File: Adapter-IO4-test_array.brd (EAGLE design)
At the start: 107.6 x 107.6 mm, 72 parts, among them CON1X11 RJ12/6, CON1X12 RJ12/6, CON1X21 RJ12/6, CON1X22 RJ12/6, CON2X11 0.100, CON2X12 0.100, CON2X21 0.100, CON2X22 0.100, Q1X11 p-fet, Q1X12 p-fet, Q1X21 p-fet, Q1X22 p-fet, Q2X11 p-fet, Q2X12 p-fet, Q2X21 p-fet, Q2X22 p-fet, Q3X11 p-fet, Q3X12 p-fet, Q3X21 p-fet, Q3X22 p-fet, Q4X11 p-fet, Q4X12 p-fet, Q4X21 p-fet, Q4X22 p-fet, SW1X11 SPST-MOM, SW1X12 SPST-MOM, SW1X21 SPST-MOM, SW1X22 SPST-MOM, SW2X11 SPST-MOM, SW2X12 SPST-MOM, SW2X21 SPST-MOM, SW2X22 SPST-MOM, SW3X11 SPST-MOM, SW3X12 SPST-MOM, SW3X21 SPST-MOM, SW3X22 SPST-MOM, SW4X11 SPST-MOM, SW4X12 SPST-MOM, SW4X21 SPST-MOM, SW4X22 SPST-MOM

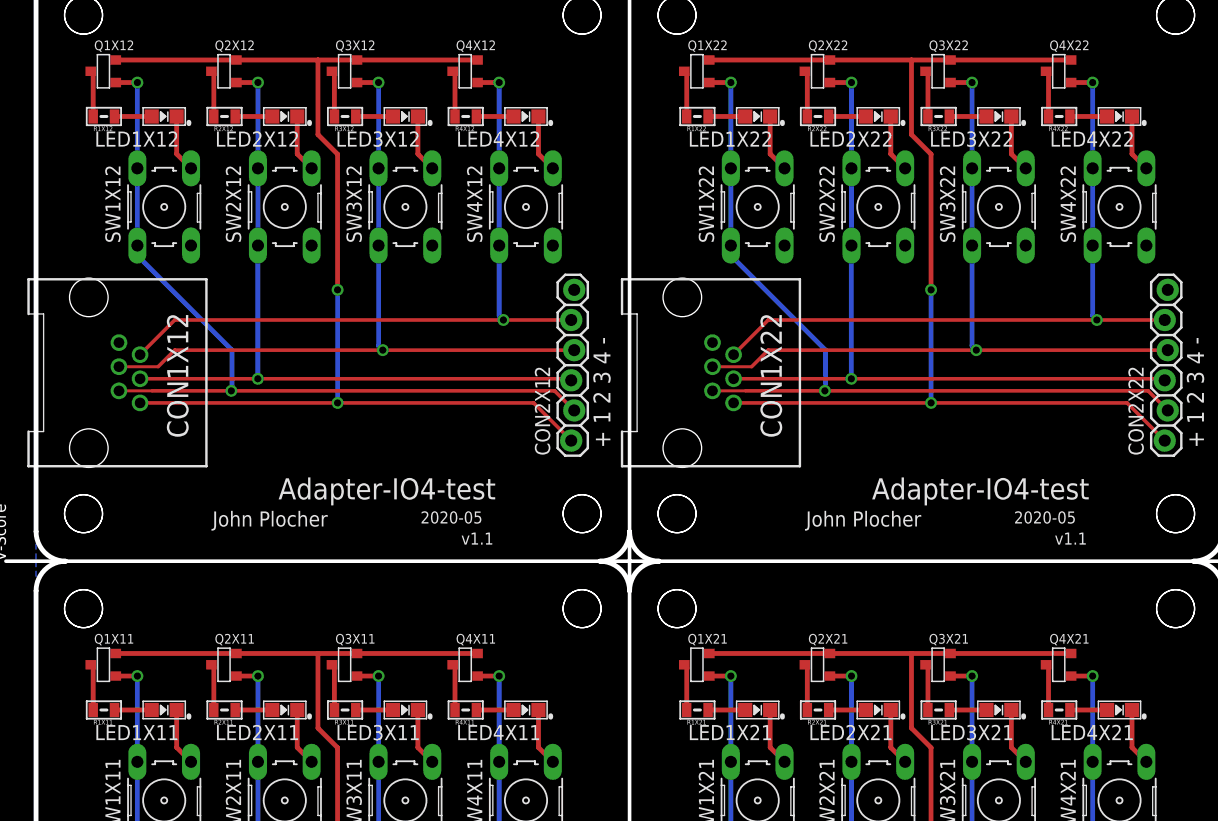
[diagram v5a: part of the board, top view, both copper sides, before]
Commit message: normalized values
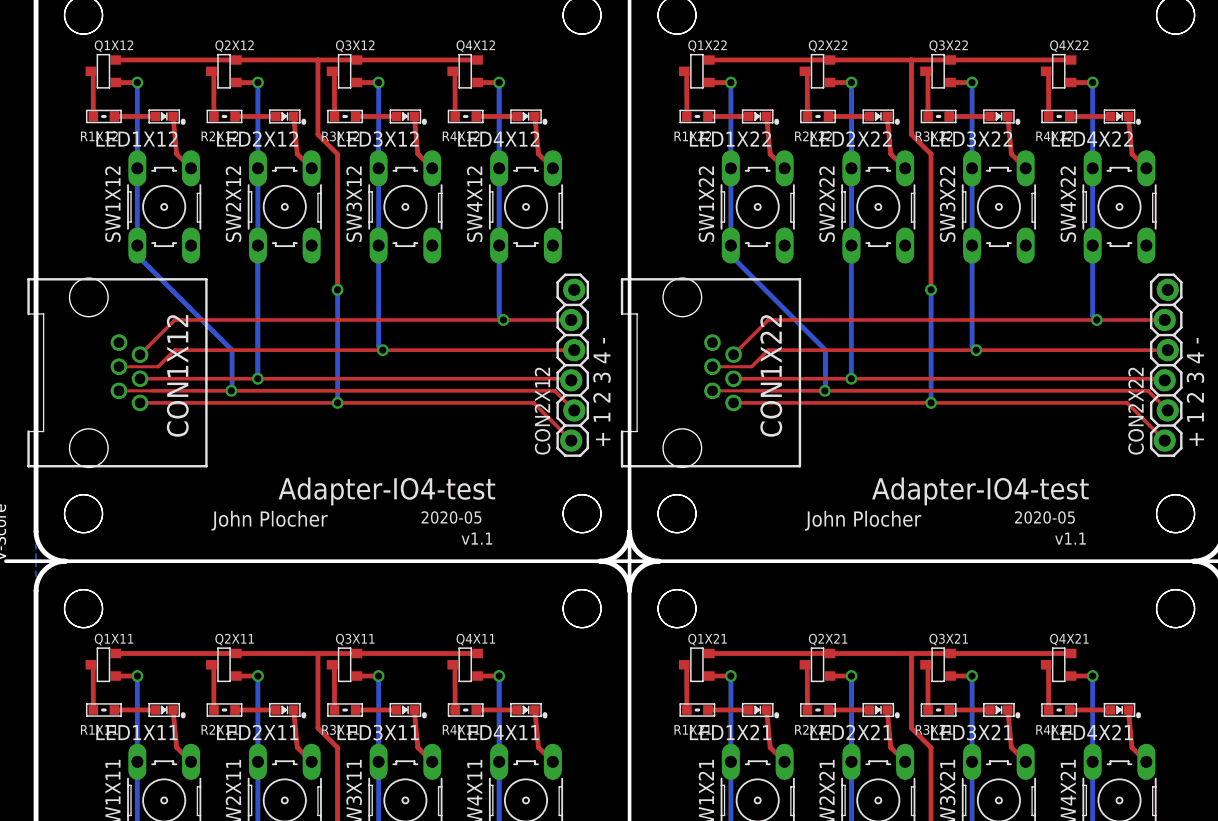
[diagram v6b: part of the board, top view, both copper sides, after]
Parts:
- LED1X11, LED1X12, LED1X21, LED1X22, LED2X11, LED2X12, LED2X21, LED2X22, LED3X11, LED3X12, LED3X21, LED3X22, LED4X11, LED4X12, LED4X21, LED4X22: device SPCoast:0805-LED -> SPCoast:0603-LED
- R1X11, R1X12, R1X21, R1X22, R2X11, R2X12, R2X21, R2X22, R3X11, R3X12, R3X21, R3X22, R4X11, R4X12, R4X21, R4X22: device SPCoast:0805-RES -> SPCoast:0603-RES
